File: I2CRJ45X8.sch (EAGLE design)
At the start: 54 parts, among them IC1 MCP23017SO, IC2 MCP23017SO, J1 M06-SOCKET, J2 M06-SOCKET, J3 M02X3-PIN, J4 M02X3-PIN, J5 RJ45-X8

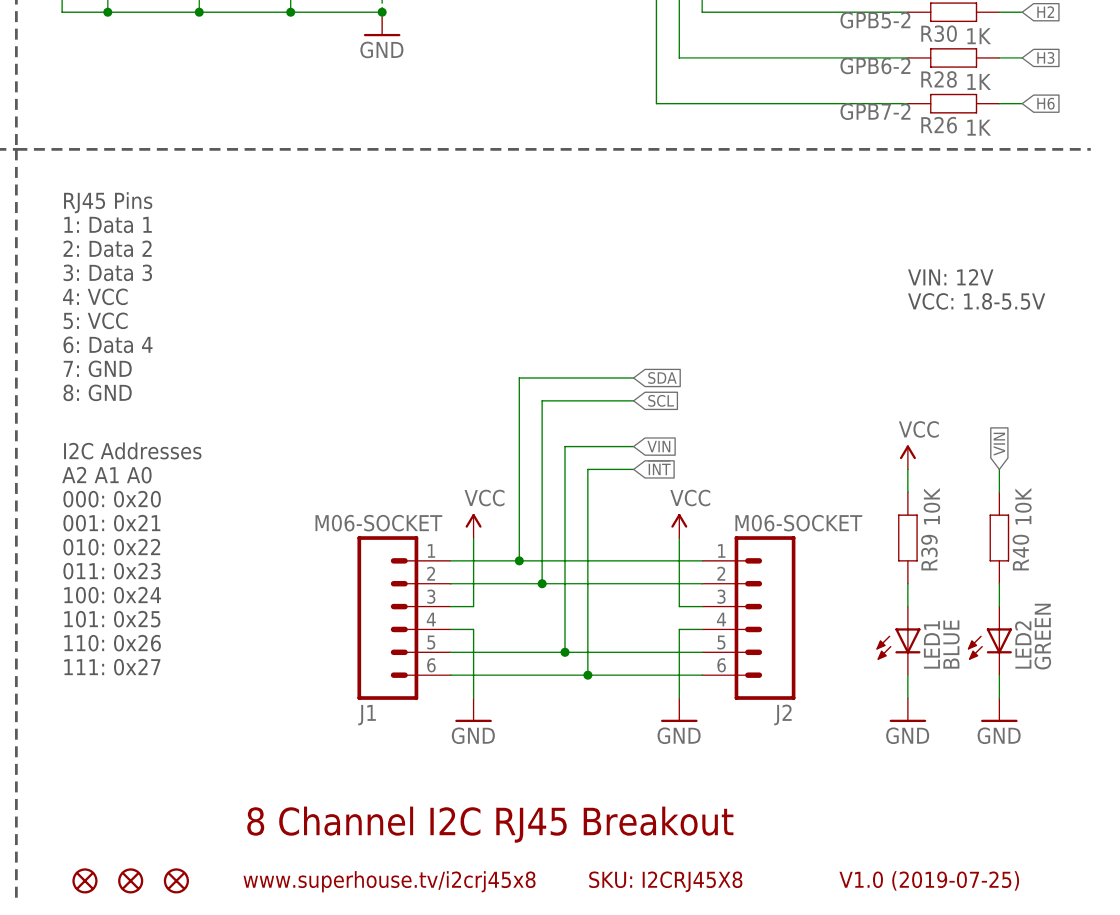
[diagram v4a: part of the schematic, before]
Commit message: Start of conversion to I2C Breakout header (2x3 shrouded)
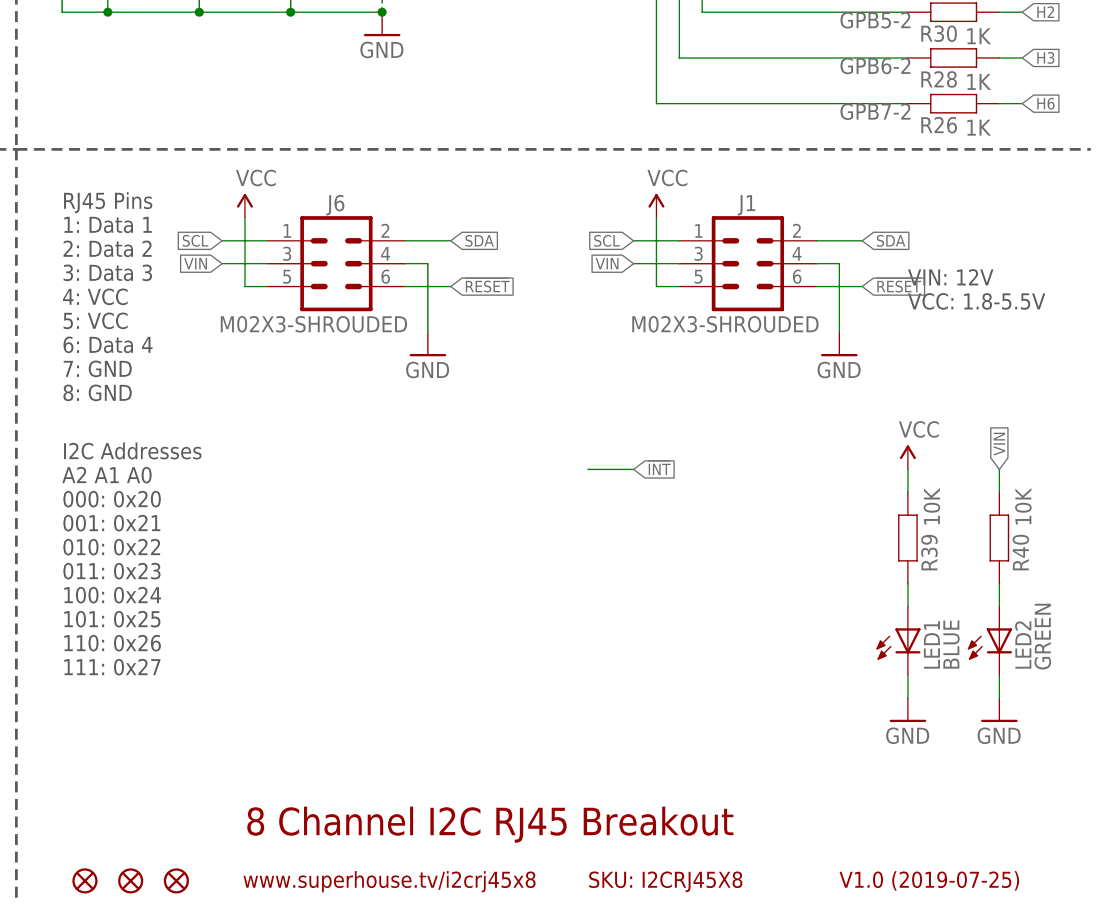
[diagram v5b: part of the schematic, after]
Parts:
- removed J2: M06-SOCKET, SuperHouse-Connectors:M06-SOCKET
- added J6: M02X3-SHROUDED, SuperHouse-Connectors:M02X3-SHROUDED
- J1: value M06-SOCKET -> M02X3-SHROUDED; device SuperHouse-Connectors:M06-SOCKET -> SuperHouse-Connectors:M02X3-SHROUDED
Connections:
- new net !RESET: J1.6, J6.6
- net !INT: no longer J1.6, J2.6
- net GND: now also J6.4; no longer J2.4
- net SCL: now also J1.1, J6.1; no longer J1.2, J2.2
- net SDA: now also J1.2, J6.2; no longer J1.1, J2.1
- net VCC: now also J1.5, J6.5; no longer J1.3, J2.3
- net VIN: now also J1.3, J6.3; no longer J1.5, J2.5
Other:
- moved on the sheet: J1

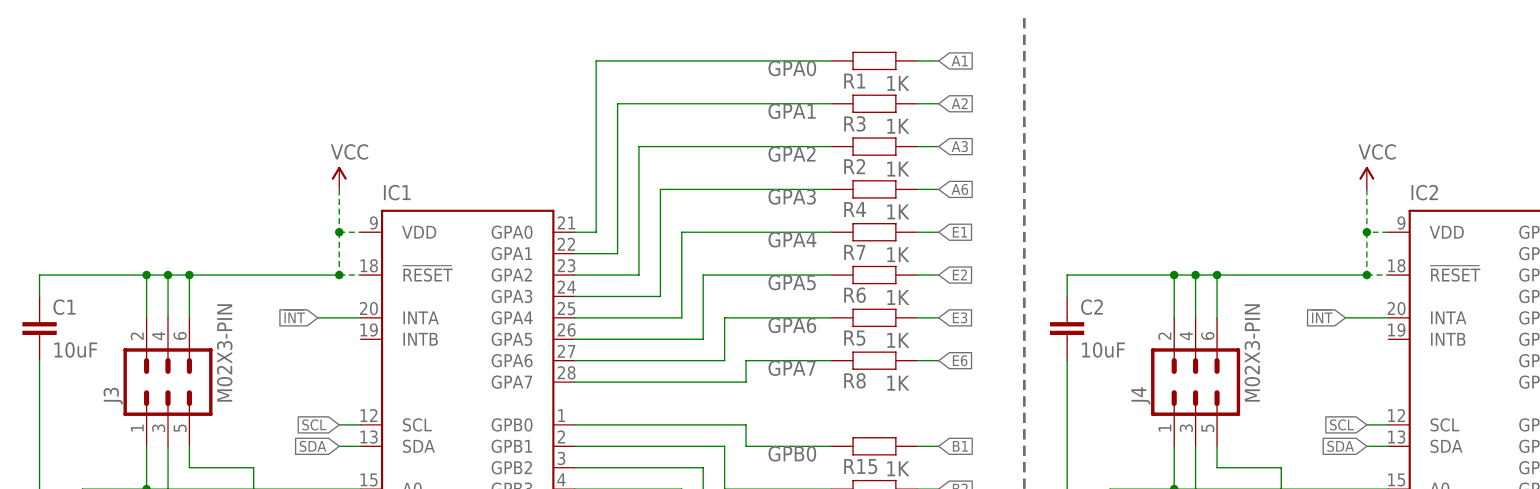
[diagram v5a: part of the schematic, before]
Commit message: Routing for I2C Breakout headers
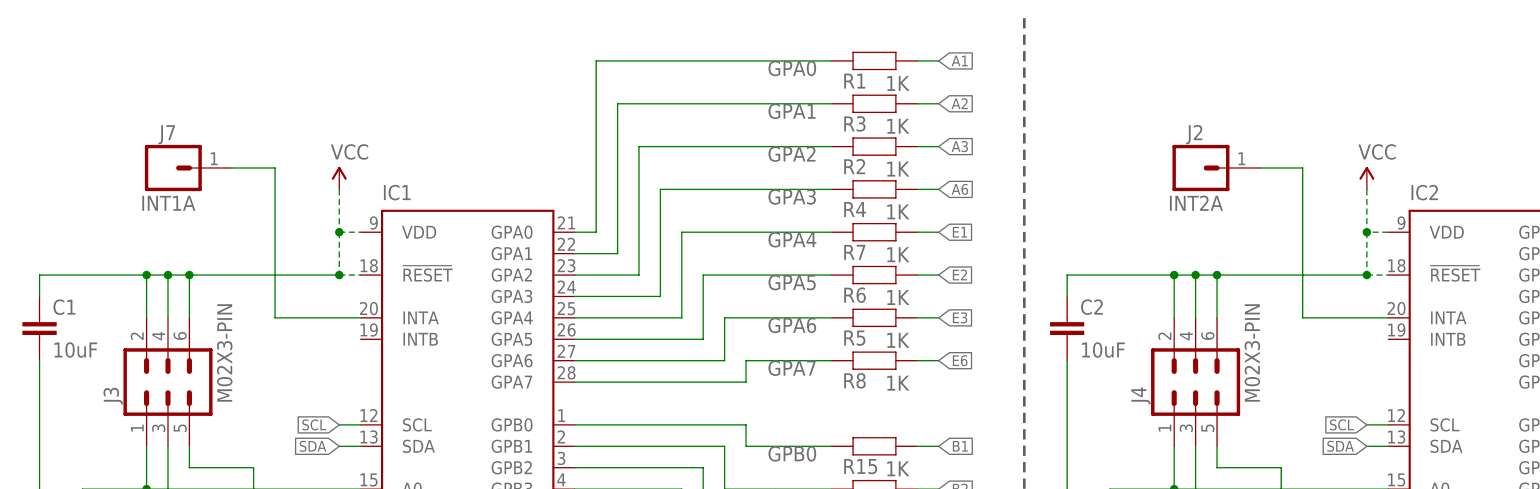
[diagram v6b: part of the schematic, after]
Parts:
- added J2: INT2A, SuperHouse-Connectors:M01-PLAIN
- added J7: INT1A, SuperHouse-Connectors:M01-PLAIN
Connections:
- removed net !INT: IC1.INTA, IC2.INTA
- new net N$10: IC1.INTA, J7.1
- new net N$9: IC2.INTA, J2.1
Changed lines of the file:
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@@
 <part name="GND4" library="SuperHouse-SupplySymbols" library_urn="urn:adsk.eagle:library:11790503" deviceset="GND" device=""/>
 <part name="P+4" library="SuperHouse-SupplySymbols" library_urn="urn:adsk.eagle:library:11790503" deviceset="VCC" device=""/>
+<part name="J2" library="SuperHouse-Connectors" library_urn="urn:adsk.eagle:library:11765989" deviceset="M01" device="-PLAIN" package3d_urn="urn:adsk.eagle:package:13097103/1" value="INT2A"/>
+<part name="J7" library="SuperHouse-Connectors" library_urn="urn:adsk.eagle:library:11765989" deviceset="M01" device="-PLAIN" package3d_urn="urn:adsk.eagle:package:13097103/1" value="INT1A"/>
 </parts>
 <sheets>
@@
 <instance part="P+4" gate="1" x="195.58" y="81.28" smashed="yes">
 <attribute name="VALUE" x="194.564" y="84.836" size="1.778" layer="96"/>
+</instance>
+<instance part="J2" gate="G$1" x="144.78" y="162.56" smashed="yes">
+<attribute name="VALUE" x="144.78" y="157.48" size="1.778" layer="96" align="bottom-center"/>
+<attribute name="NAME" x="144.78" y="165.862" size="1.778" layer="95" align="bottom-center"/>
+</instance>
+<instance part="J7" gate="G$1" x="22.86" y="162.56" smashed="yes">
+<attribute name="VALUE" x="22.86" y="157.48" size="1.778" layer="96" align="bottom-center"/>
+<attribute name="NAME" x="22.86" y="165.862" size="1.778" layer="95" align="bottom-center"/>
 </instance>
 </instances>
@@
 <label x="193.04" y="53.34" size="1.27" layer="95" xref="yes"/>
 </segment>
-<segment>
-<pinref part="IC1" gate="G$1" pin="INTA"/>
-<wire x1="45.72" y1="144.78" x2="40.64" y2="144.78" width="0.1524" layer="91"/>
-<label x="40.64" y="144.78" size="1.27" layer="95" rot="R180" xref="yes"/>
-</segment>
-<segment>
-<pinref part="IC2" gate="G$1" pin="INTA"/>
-<wire x1="167.64" y1="144.78" x2="162.56" y2="144.78" width="0.1524" layer="91"/>
-<label x="162.56" y="144.78" size="1.27" layer="95" rot="R180" xref="yes"/>
-</segment>
 </net>
 <net name="N$1" class="0">
@@
 </segment>
 </net>
+<net name="N$9" class="0">
+<segment>
+<pinref part="IC2" gate="G$1" pin="INTA"/>
+<wire x1="167.64" y1="144.78" x2="157.48" y2="144.78" width="0.1524" layer="91"/>
+<wire x1="157.48" y1="144.78" x2="157.48" y2="162.56" width="0.1524" layer="91"/>
+<pinref part="J2" gate="G$1" pin="1"/>
+<wire x1="157.48" y1="162.56" x2="152.4" y2="162.56" width="0.1524" layer="91"/>
+</segment>
+</net>
+<net name="N$10" class="0">
+<segment>
+<pinref part="IC1" gate="G$1" pin="INTA"/>
+<wire x1="45.72" y1="144.78" x2="35.56" y2="144.78" width="0.1524" layer="91"/>
+<wire x1="35.56" y1="144.78" x2="35.56" y2="162.56" width="0.1524" layer="91"/>
+<pinref part="J7" gate="G$1" pin="1"/>
+<wire x1="35.56" y1="162.56" x2="30.48" y2="162.56" width="0.1524" layer="91"/>
+</segment>
+</net>

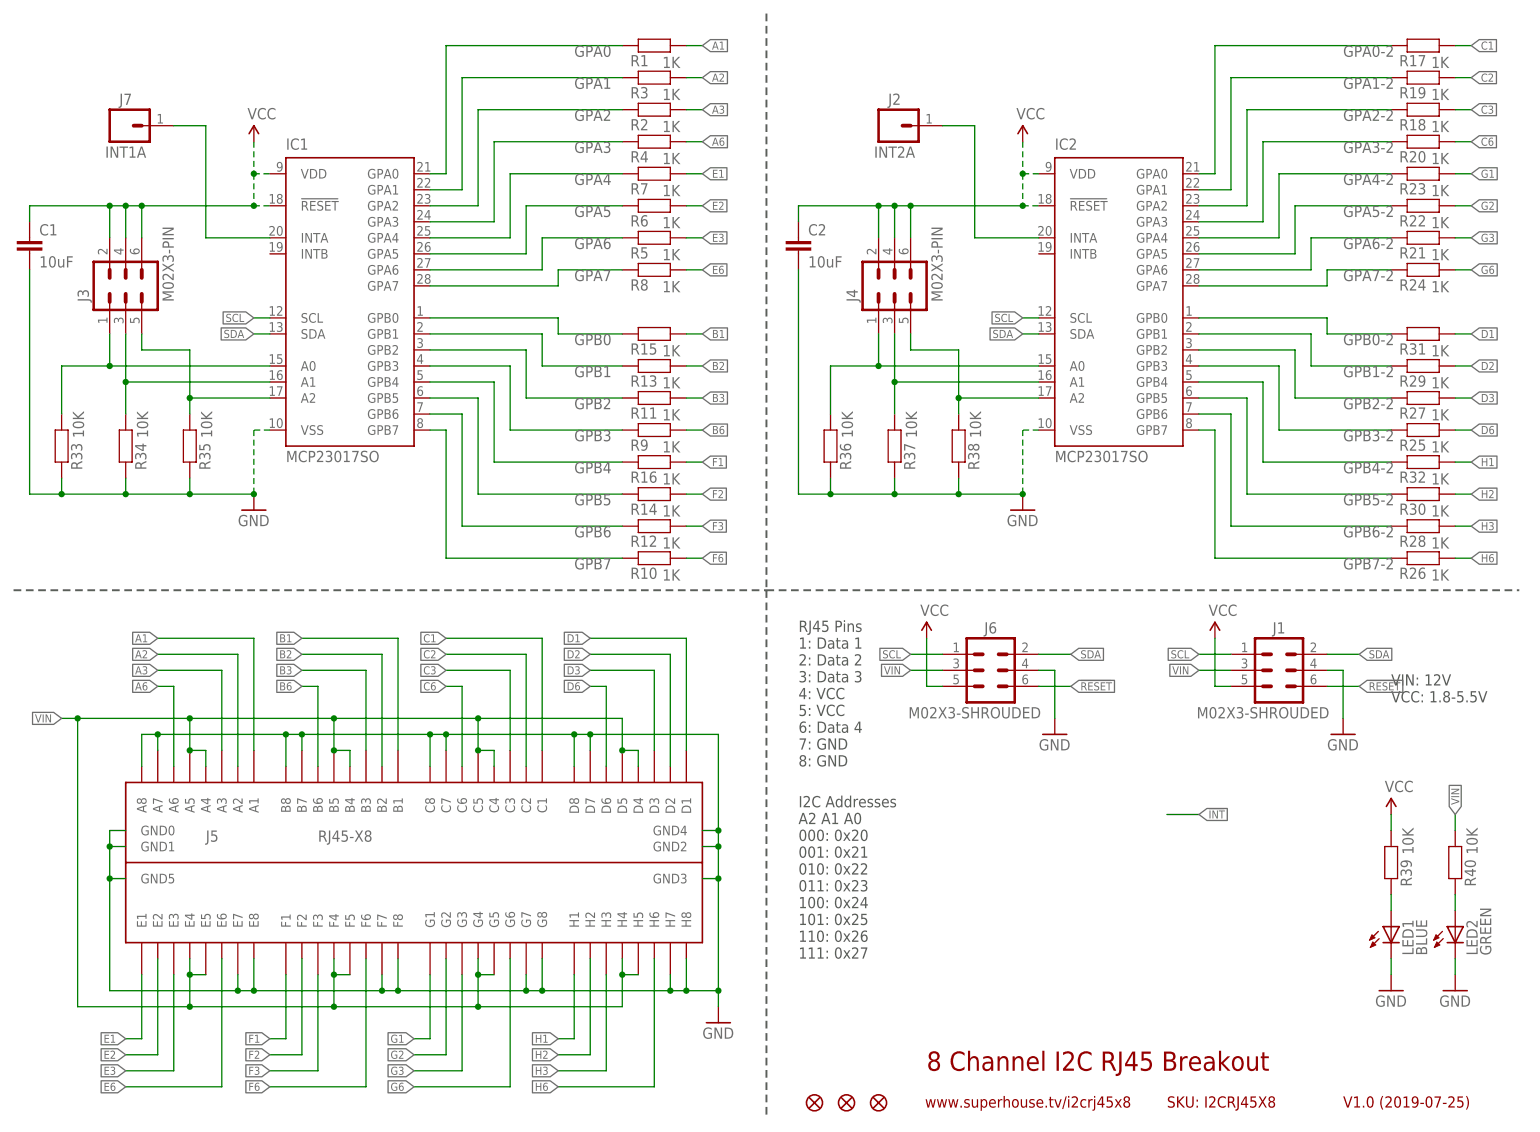
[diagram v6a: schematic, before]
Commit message: Experimenting with options for linking MCP reset to I2C Breakout reset
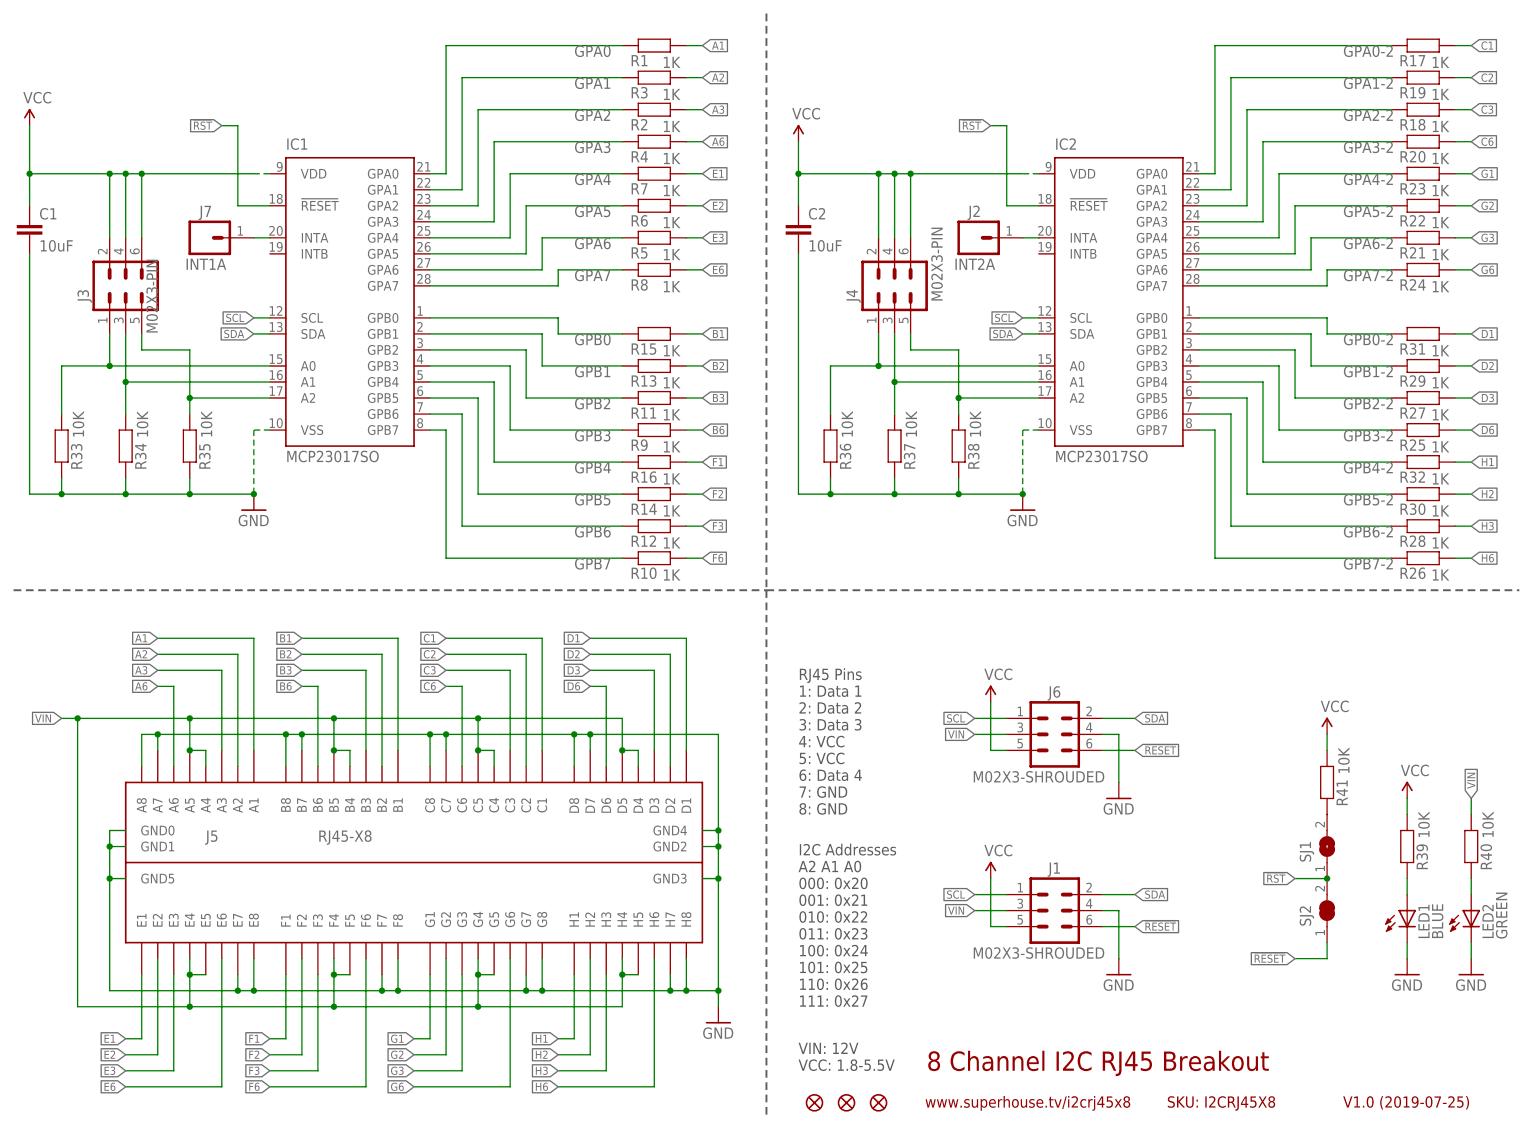
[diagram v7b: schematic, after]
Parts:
- added R41: 10K, SuperHouse-DiscreteSemi:RESISTOR0603
- added SJ1: (no value), SuperHouse-Jumpers:SJ-NORMAL
- added SJ2: SJC-NORMAL, SuperHouse-Jumpers:SJC-NORMAL
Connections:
- new net !RST: IC1.!RESET, IC2.!RESET, SJ1.1, SJ2.2
- new net N$14: R41.1, SJ1.2
- net !RESET: now also SJ2.1
- net VCC: now also R41.2; no longer IC1.!RESET, IC2.!RESET
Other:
- moved on the sheet: C1, C2, J1, J2, J6, J7, LED1, LED2, R39, R40
